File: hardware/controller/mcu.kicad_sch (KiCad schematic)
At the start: 21 parts, among them J12 USB_C_Receptacle_USB2.0_14P, J5 Screw_Terminal_01x02, J6 Screw_Terminal_01x02, U1 ESP32-C3-MINI-1, U6 TPS1H200AQDGNRQ1

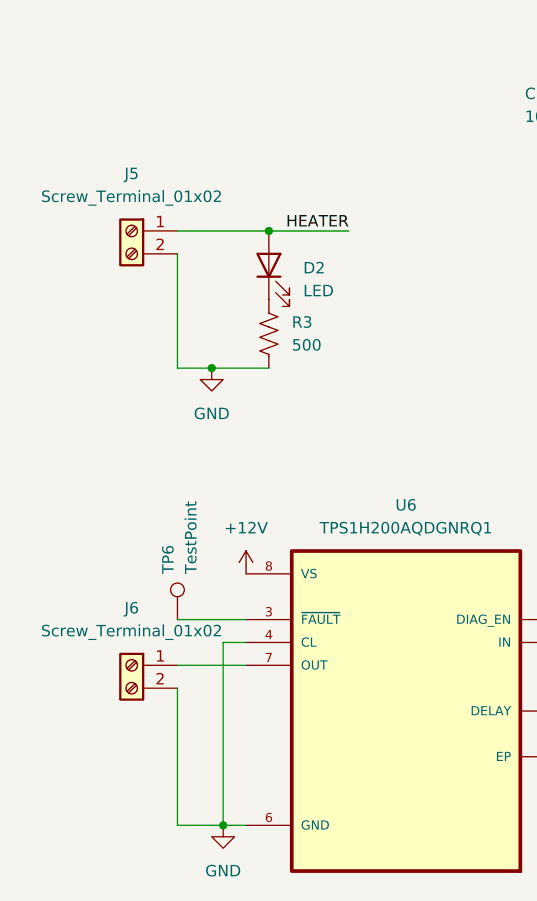
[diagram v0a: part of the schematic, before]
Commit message: Widen board and add polarity labels to heater outputs
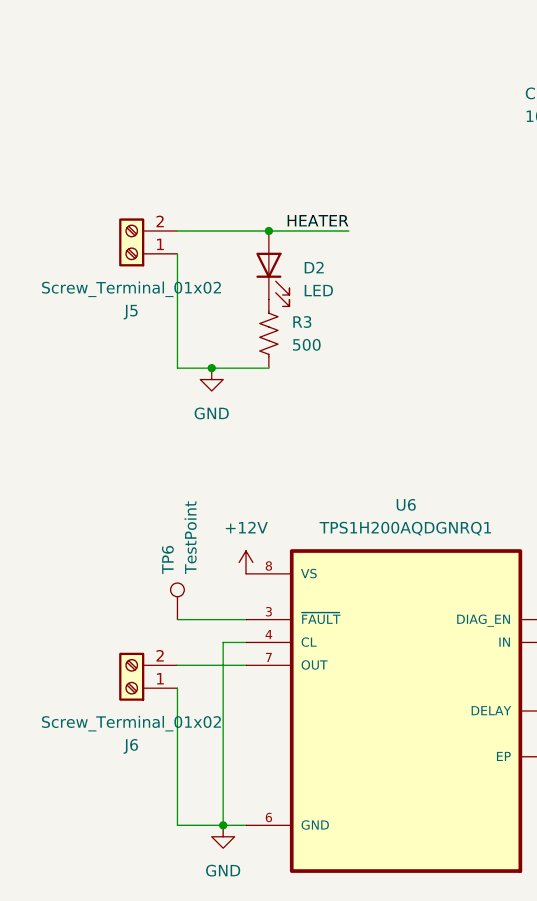
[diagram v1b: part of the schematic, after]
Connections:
- net GND: now also J5.1 (Pin_1), J6.1 (Pin_1); no longer J5.2 (Pin_2), J6.2 (Pin_2)
- net HEATER: now also J5.2 (Pin_2); no longer J5.1 (Pin_1)
- net at U6.7 (OUT): now also J6.2 (Pin_2); no longer J6.1 (Pin_1)
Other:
- moved on the sheet: J5, J6
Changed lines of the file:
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@@
 	(symbol
 		(lib_id "Connector:Screw_Terminal_01x02")
-		(at 49.53 137.16 0)
-		(mirror y)
-		(unit 1)
-		(exclude_from_sim no)
-		(in_bom yes)
-		(on_board yes)
-		(dnp no)
-		(fields_autoplaced yes)
+		(at 49.53 139.7 180)
+		(unit 1)
+		(exclude_from_sim no)
+		(in_bom yes)
+		(on_board yes)
+		(dnp no)
 		(property "Reference" "J6"
-			(at 49.53 130.81 0)
+			(at 49.53 146.05 0)
 			(effects
 				(font
@@
 		)
 		(property "Value" "Screw_Terminal_01x02"
-			(at 49.53 133.35 0)
+			(at 49.53 143.51 0)
 			(effects
 				(font
@@
 		)
 		(property "Footprint" "TerminalBlock_4Ucon:TerminalBlock_4Ucon_1x02_P3.50mm_Horizontal"
-			(at 49.53 137.16 0)
+			(at 49.53 139.7 0)
 			(effects
 				(font
@@
 		)
 		(property "Datasheet" "~"
-			(at 49.53 137.16 0)
+			(at 49.53 139.7 0)
 			(effects
 				(font
@@
 		)
 		(property "Description" "Generic screw terminal, single row, 01x02, script generated (kicad-library-utils/schlib/autogen/connector/)"
-			(at 49.53 137.16 0)
+			(at 49.53 139.7 0)
 			(effects
 				(font
@@
 	(symbol
 		(lib_id "Connector:Screw_Terminal_01x02")
-		(at 49.53 88.9 0)
-		(mirror y)
-		(unit 1)
-		(exclude_from_sim no)
-		(in_bom yes)
-		(on_board yes)
-		(dnp no)
-		(fields_autoplaced yes)
+		(at 49.53 91.44 180)
+		(unit 1)
+		(exclude_from_sim no)
+		(in_bom yes)
+		(on_board yes)
+		(dnp no)
 		(property "Reference" "J5"
-			(at 49.53 82.55 0)
+			(at 49.53 97.79 0)
 			(effects
 				(font
@@
 		)
 		(property "Value" "Screw_Terminal_01x02"
-			(at 49.53 85.09 0)
+			(at 49.53 95.25 0)
 			(effects
 				(font
@@
 		)
 		(property "Footprint" "TerminalBlock_4Ucon:TerminalBlock_4Ucon_1x02_P3.50mm_Horizontal"
-			(at 49.53 88.9 0)
+			(at 49.53 91.44 0)
 			(effects
 				(font
@@
 		)
 		(property "Datasheet" "~"
-			(at 49.53 88.9 0)
+			(at 49.53 91.44 0)
 			(effects
 				(font
@@
 		)
 		(property "Description" "Generic screw terminal, single row, 01x02, script generated (kicad-library-utils/schlib/autogen/connector/)"
-			(at 49.53 88.9 0)
-			(effects
-				(font
+			(at 49.53 91.44 0)
+			(effects
+				(font

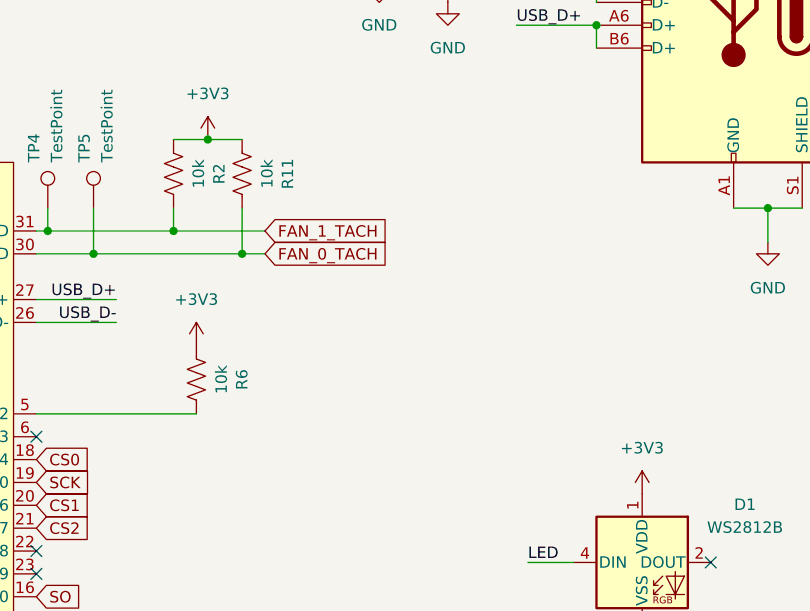
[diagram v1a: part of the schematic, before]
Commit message: Protect fan tach inputs
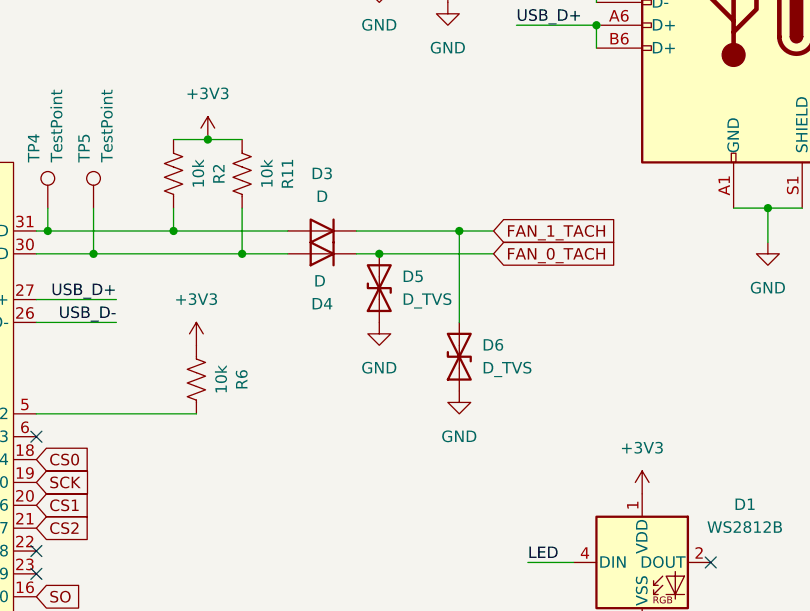
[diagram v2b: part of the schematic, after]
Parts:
- added D3, D4: D, Package_TO_SOT_SMD:TSOT-23, symbol Device:D
- added D5, D6: D_TVS, Diode_SMD:D_SOD-323F, symbol Device:D_TVS
- TP4, TP5: now left out of the parts list
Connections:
- net FAN_0_TACH: now also D4.1 (K), D5.2 (A2); no longer R11.1, TP5.1, U1.30 (GPIO20/U0RXD)
- net FAN_1_TACH: now also D3.1 (K), D6.2 (A2); no longer R2.1, TP4.1, U1.31 (GPIO21/U0TXD)
- net GND: now also D5.1 (A1), D6.1 (A1)
- new net: D3.2 (A), R2.1, TP4.1, U1.31 (GPIO21/U0TXD)
- new net: D4.2 (A), R11.1, TP5.1, U1.30 (GPIO20/U0RXD)

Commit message: Increase via size for manufacturing
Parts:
- TP6: now left out of the parts list
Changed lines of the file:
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@@
 		(unit 1)
 		(exclude_from_sim no)
-		(in_bom yes)
+		(in_bom no)
 		(on_board yes)
 		(dnp no)

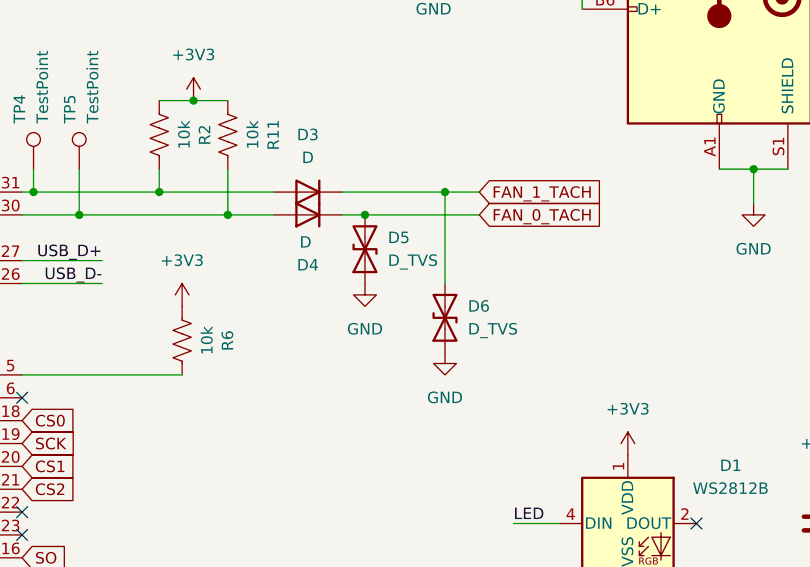
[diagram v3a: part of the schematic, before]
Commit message: Fix diode footprints
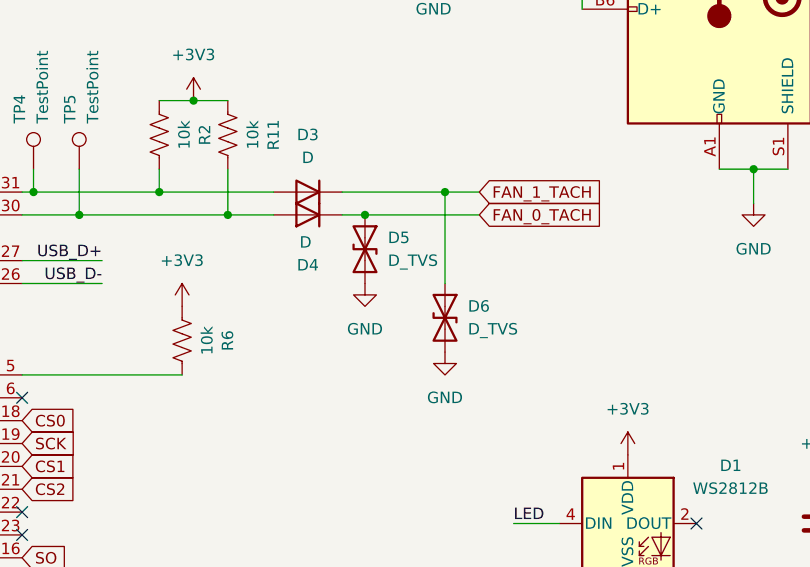
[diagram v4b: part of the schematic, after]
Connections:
- net FAN_0_TACH: now also D4.3 (K), D5.1 (A1); no longer D4.1 (K), D5.2 (A2)
- net FAN_1_TACH: now also D3.3 (K), D6.1 (A1); no longer D3.1 (K), D6.2 (A2)
- net GND: now also D5.2 (A2), D6.2 (A2); no longer D5.1 (A1), D6.1 (A1)
- net at R2.1, TP4.1, U1.31 (GPIO21/U0TXD): now also D3.1 (A); no longer D3.2 (A)
- net at R11.1, TP5.1, U1.30 (GPIO20/U0RXD): now also D4.1 (A); no longer D4.2 (A)
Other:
- moved on the sheet: D5, D6
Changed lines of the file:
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@@
 	)
 	(junction
-		(at 212.09 77.47)
-		(diameter 0)
-		(color 0 0 0 0)
-	)
-	(junction
 		(at 146.05 48.26)
 		(diameter 0)
@@
 	)
 	(junction
+		(at 212.09 77.47)
+		(diameter 0)
+		(color 0 0 0 0)
+	)
+	(junction
 		(at 58.42 104.14)
 		(diameter 0)
@@
 	(wire
 		(pts
-			(xy 212.09 77.47) (xy 224.79 77.47)
-		)
-		(stroke
-			(width 0)
-			(type default)
-		)
-	)
-	(wire
-		(pts
 			(xy 219.71 41.91) (xy 236.22 41.91)
 		)
@@
 	(wire
 		(pts
+			(xy 212.09 77.47) (xy 224.79 77.47)
+		)
+		(stroke
+			(width 0)
+			(type default)
+		)
+	)
+	(wire
+		(pts
 			(xy 189.23 74.93) (xy 201.93 74.93)
 		)
@@
 	(symbol
 		(lib_id "Device:D_TVS")
-		(at 220.98 88.9 90)
+		(at 220.98 88.9 270)
 		(unit 1)
 		(exclude_from_sim no)
@@
 					(size 1.27 1.27)
 				)
-				(justify right)
+				(justify left)
 			)
 		)
@@
 					(size 1.27 1.27)
 				)
-				(justify right)
+				(justify left)
 			)
 		)
@@
 		(pin "1"
 		)
-		(pin "2"
+		(pin "3"
 		)
 		(instances
@@
 	)
 	(symbol
+		(lib_name "D_1")
 		(lib_id "Device:D")
 		(at 205.74 74.93 180)
@@
 			)
 		)
-		(pin "2"
+		(pin "3"
 		)
 		(pin "1"
@@
 	(symbol
 		(lib_id "Device:D_TVS")
-		(at 212.09 81.28 90)
+		(at 212.09 81.28 270)
 		(unit 1)
 		(exclude_from_sim no)
@@
 					(size 1.27 1.27)
 				)
-				(justify right)
+				(justify left)
 			)
 		)
@@
 					(size 1.27 1.27)
 				)
-				(justify right)
+				(justify left)
 			)
 		)
